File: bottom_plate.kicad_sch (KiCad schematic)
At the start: 27 parts, among them J42 Osc Out, J43 Conn_02x08_Odd_Even, J44 Conn_02x08_Odd_Even, J45 Conn_02x08_Odd_Even, J46 Conn_02x08_Odd_Even, J47 Conn_02x08_Odd_Even, J48 Select, J49 Select, J60 VCC, J61 VCC, J62 GND, J63 GND, J64 Conn_02x08_Odd_Even, J66 4017 Pins, J67 4017 Pins, J73 Conn_02x20_Odd_Even, J74 Conn_02x20_Odd_Even, J75 Conn_02x20_Odd_Even, J76 Conn_02x20_Odd_Even, J77 Conn_02x20_Odd_Even, J78 Conn_02x20_Odd_Even, J79 Conn_02x20_Odd_Even, J80 Conn_02x20_Odd_Even, J81 Conn_02x20_Odd_Even, J85 Output, J86 Output, J88 Conn_01x18

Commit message: start smd refactoring
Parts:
- J88: KiLib_Generator (none) -> connector/pin_header_socket
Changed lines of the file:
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@@
+			)
+		)
+		(property "KiLib_Generator" "connector/pin_header_socket"
+			(at 260.35 64.77 0)
+			(hide yes)
+			(show_name no)
+			(do_not_autoplace no)
+			(effects
+				(font
+					(size 1.27 1.27)
+				)
 			)
 		)

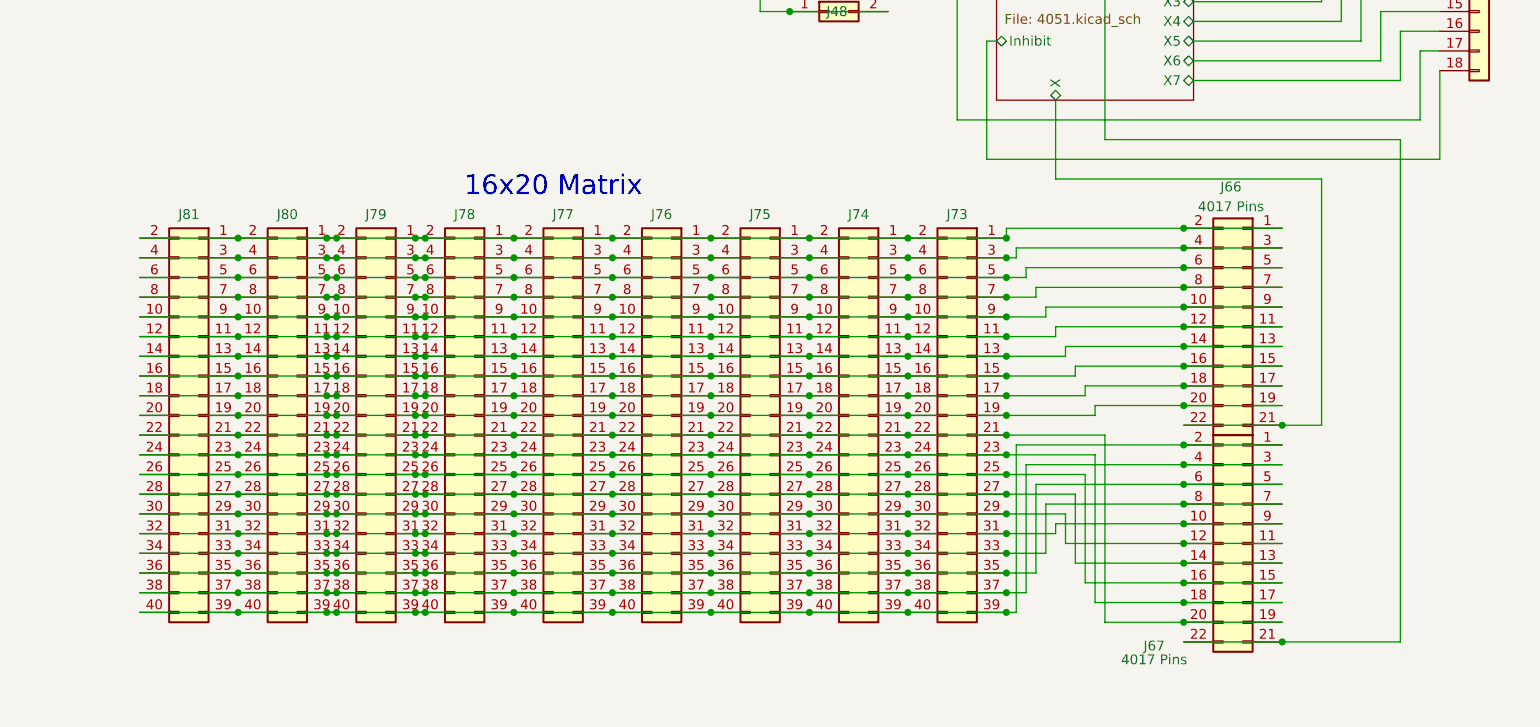
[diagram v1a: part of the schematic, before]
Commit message: clear all components, geometric constraints
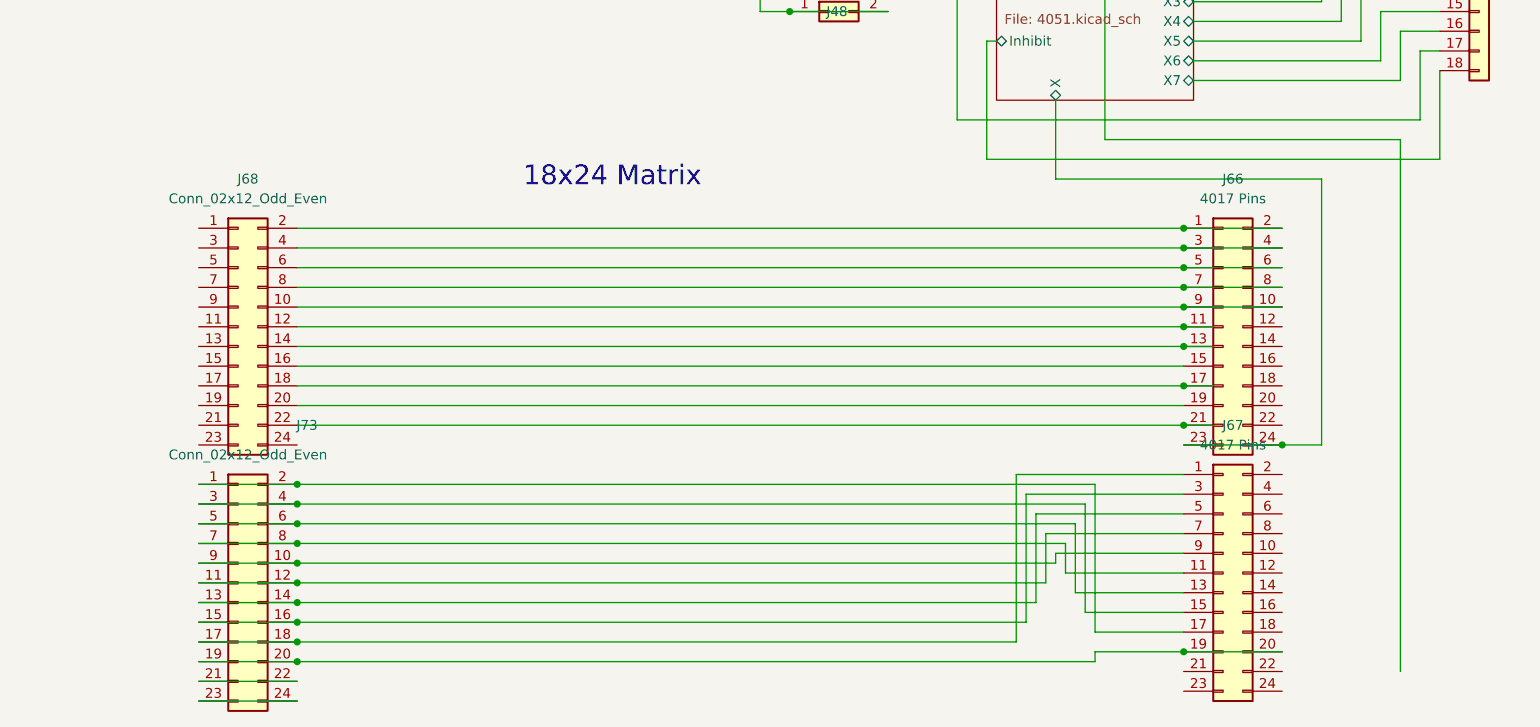
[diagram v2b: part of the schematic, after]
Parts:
- removed J66, J67: 4017 Pins, Connector_PinSocket_2.54mm:PinSocket_2x11_P2.54mm_Vertical, symbol Connector_Generic:Conn_02x11_Odd_Even
- removed J73, J74, J75, J76, J77, J78, J79, J80, J81: Conn_02x20_Odd_Even, Connector_PinHeader_2.54mm:PinHeader_2x20_P2.54mm_Vertical, symbol Connector_Generic:Conn_02x20_Odd_Even
- added J66, J67: 4017 Pins, Connector_PinSocket_2.54mm:PinSocket_2x12_P2.54mm_Vertical, symbol Connector_Generic:Conn_02x12_Odd_Even
- added J68, J73: Conn_02x12_Odd_Even, kleingorium:Header_2x12_P2.54mm_Vertical_SMD_FH-00369, symbol Connector_Generic:Conn_02x12_Odd_Even
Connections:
- net 4051 2/X: now also J66.23 (Pin_23), J66.24 (Pin_24)
- new net: J67.17 (Pin_17), J73.1 (Pin_1), J73.2 (Pin_2)
- new net: J67.9 (Pin_9), J73.10 (Pin_10), J73.9 (Pin_9)
- new net: J67.7 (Pin_7), J73.11 (Pin_11), J73.12 (Pin_12)
- new net: J67.5 (Pin_5), J73.13 (Pin_13), J73.14 (Pin_14)
- new net: J67.3 (Pin_3), J73.15 (Pin_15), J73.16 (Pin_16)
- new net: J67.1 (Pin_1), J73.17 (Pin_17), J73.18 (Pin_18)
- new net: J67.19 (Pin_19), J67.20 (Pin_20), J73.19 (Pin_19), J73.20 (Pin_20)
- new net: J73.21 (Pin_21), J73.22 (Pin_22)
- new net: J73.23 (Pin_23), J73.24 (Pin_24)
- new net: J67.15 (Pin_15), J73.3 (Pin_3), J73.4 (Pin_4)
- new net: J67.13 (Pin_13), J73.5 (Pin_5), J73.6 (Pin_6)
- new net: J67.11 (Pin_11), J73.7 (Pin_7), J73.8 (Pin_8)
- new net: J66.1 (Pin_1), J66.2 (Pin_2), J68.2 (Pin_2)
- new net: J66.10 (Pin_10), J66.9 (Pin_9), J68.10 (Pin_10)
- new net: J66.11 (Pin_11), J68.12 (Pin_12)
- new net: J66.13 (Pin_13), J68.14 (Pin_14)
- new net: J66.15 (Pin_15), J68.16 (Pin_16)
- new net: J66.17 (Pin_17), J68.18 (Pin_18)
- new net: J66.19 (Pin_19), J68.20 (Pin_20)
- new net: J66.21 (Pin_21), J68.22 (Pin_22)
- new net: J66.3 (Pin_3), J66.4 (Pin_4), J68.4 (Pin_4)
- new net: J66.5 (Pin_5), J66.6 (Pin_6), J68.6 (Pin_6)
- new net: J66.7 (Pin_7), J66.8 (Pin_8), J68.8 (Pin_8)
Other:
- note added: "18x24 Matrix"
- note removed: "16x20 Matrix"
